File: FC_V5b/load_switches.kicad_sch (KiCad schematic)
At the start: 48 parts, among them U19 AP22652, U21 AP22652, U22 AP22652, U23 AP22652, U24 AP22652, U25 TPS2HB50AQPWPRQ1, U29 AP22652, U6 TPS4H160AQPWPRQ1

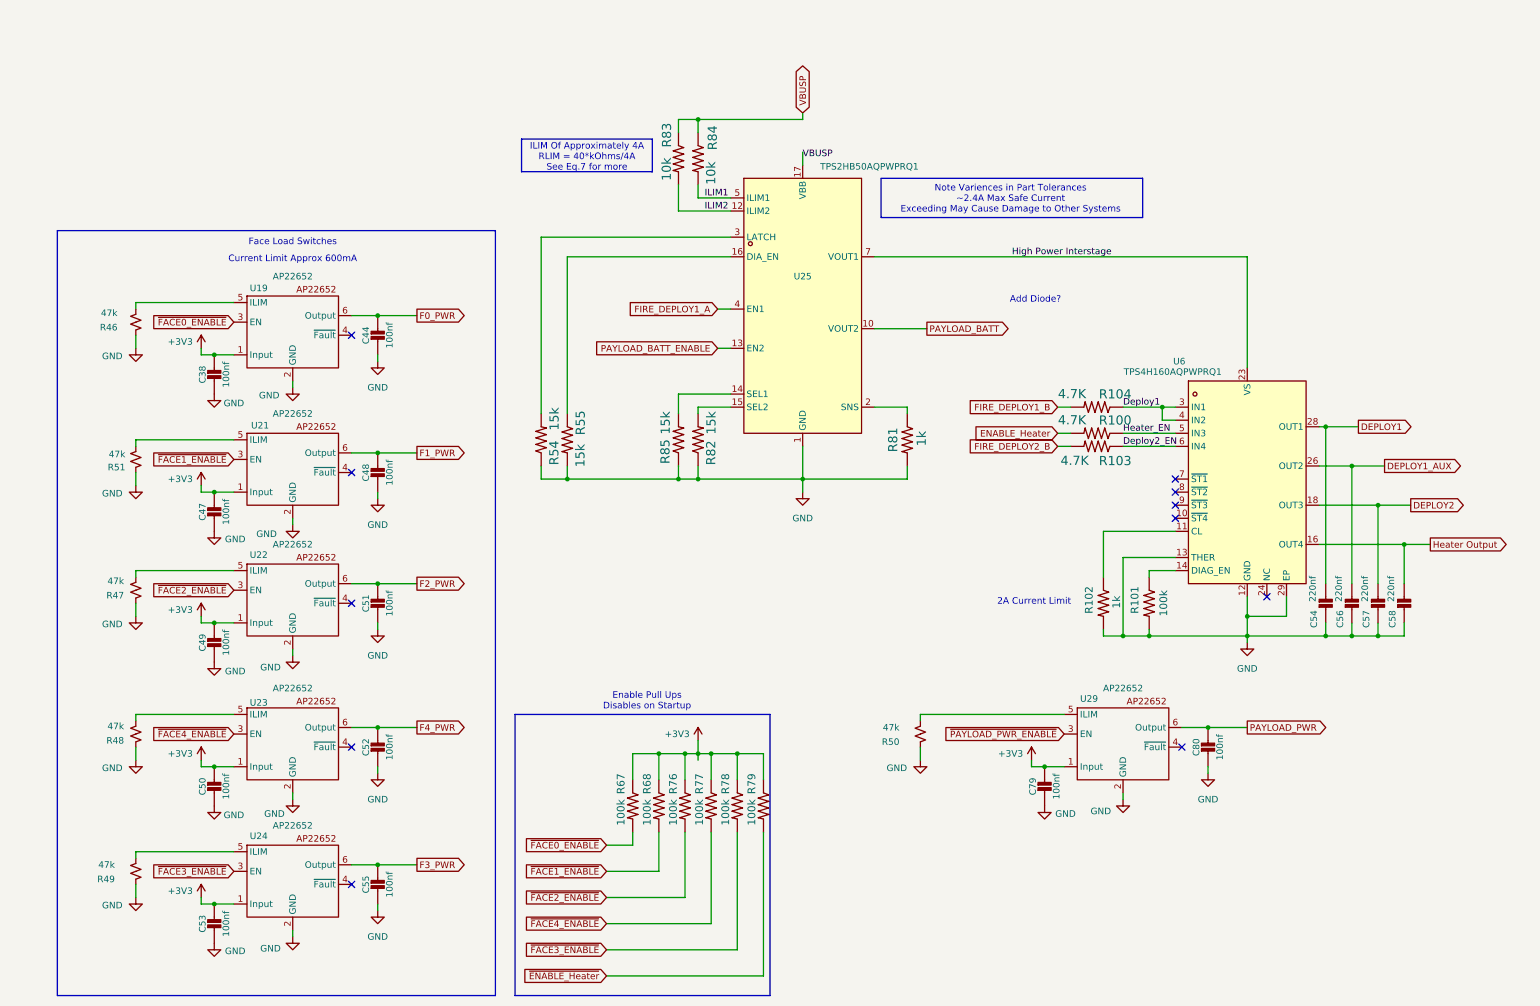
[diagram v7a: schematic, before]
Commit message: Changed to AP22653AW6-7 Load Switches for EN High
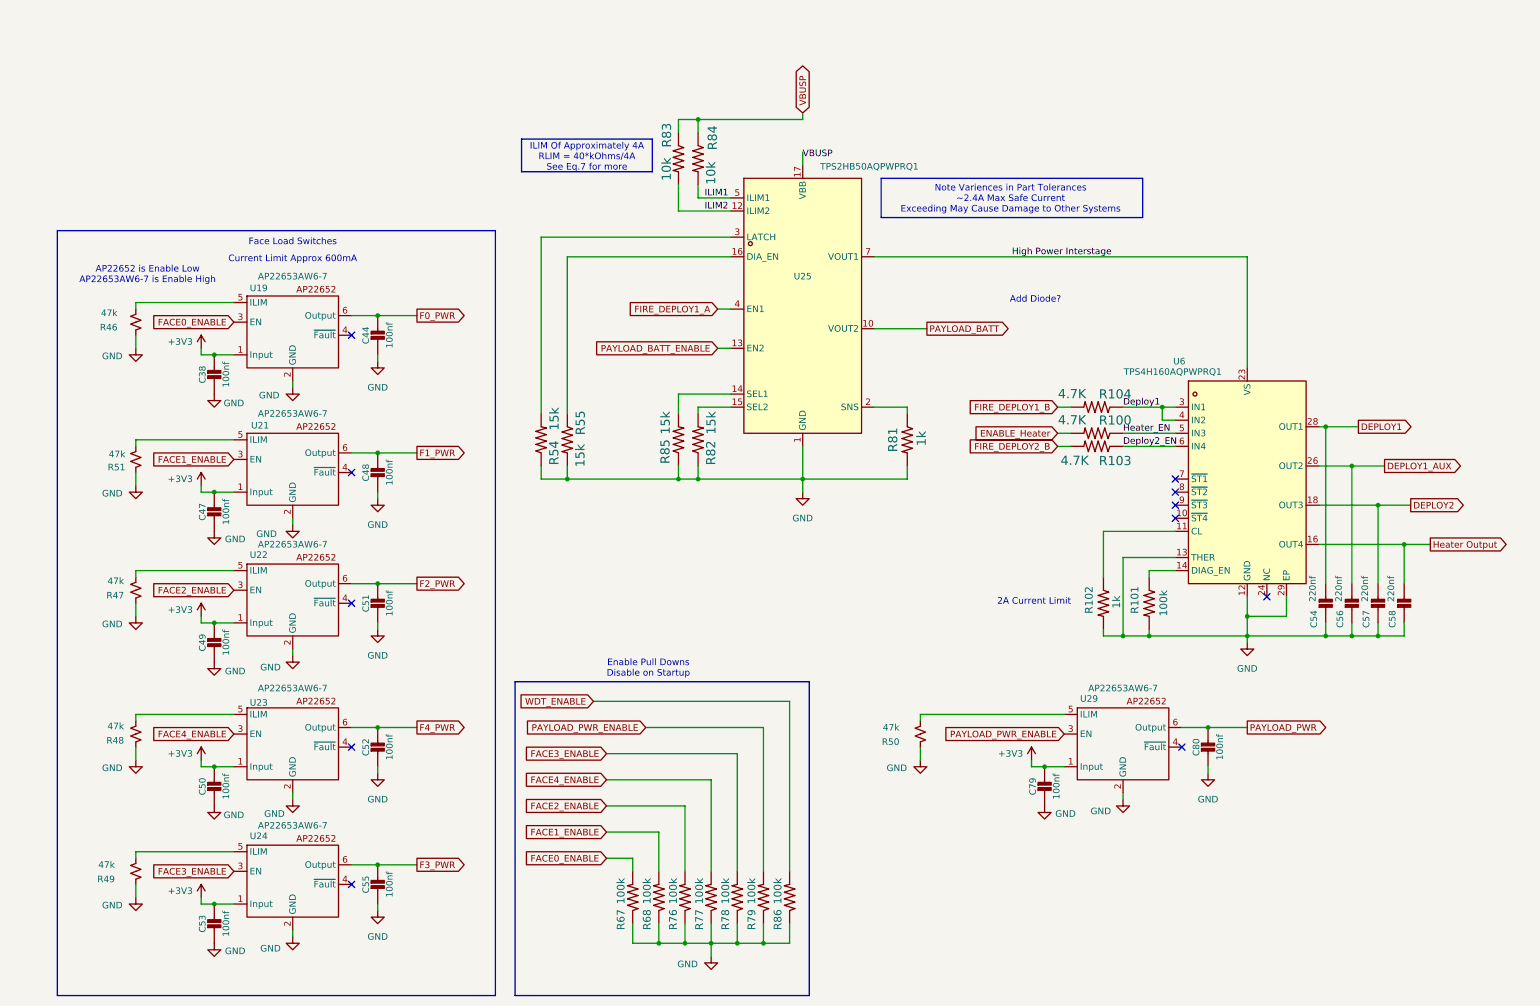
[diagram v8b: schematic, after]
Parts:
- added R86: 100k, Resistor_SMD:R_0603_1608Metric, symbol mainboard:R-US_R0603
- U19, U21, U22, U23, U24, U29: value AP22652 -> AP22653AW6-7
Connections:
- net ~{PAYLOAD_PWR_ENABLE} is gone; now on net PAYLOAD_PWR_ENABLE: U29.3 (EN)
- net +3V3: no longer R67.1, R68.1, R76.1, R77.1, R78.1, R79.1
- net GND: now also R67.1, R68.1, R76.1, R77.1, R78.1, R79.1, R86.1
- net ~{ENABLE_Heater} renamed PAYLOAD_PWR_ENABLE
- net ~{FACE0_ENABLE} renamed FACE0_ENABLE
- net ~{FACE1_ENABLE} renamed FACE1_ENABLE
- net ~{FACE2_ENABLE} renamed FACE2_ENABLE
- net ~{FACE3_ENABLE} renamed FACE3_ENABLE
- net ~{FACE4_ENABLE} renamed FACE4_ENABLE
- new net WDT_ENABLE: R86.2
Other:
- note added: "AP22652 is Enable Low AP22653AW6-7 is Enable High"
- note added: "Enable Pull Downs Disable on Startup"
- note removed: "Enable Pull Ups Disables on Startup"
- moved on the sheet: R67, R68, R76, R77, R78, R79
